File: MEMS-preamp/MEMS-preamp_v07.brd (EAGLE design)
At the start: 50 x 30.1 mm, 45 parts, among them IC1 DMN2400, IC2 BQ21040, IC3 BQ297X, IC4 SC4503, IC5 TPS7A49, IC6 OPA2134, J2 Battery, SW1 SPDT

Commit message: boards layed out
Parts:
- C1, C10, C2, C3, C7, C8: device adafruit:C0603 -> rcl:C0603
- C4: value 56nf -> 56nF; device adafruit:C0603 -> rcl:C0603
- C5: value 2.2pf -> 2.2pF; device adafruit:C0603 -> rcl:C0603
- C6: device SparkFun:EIA3528 -> rcl:C1206
- C9: value 10nF -> 10uF; device adafruit:C0603 -> rcl:C0603
- moved C6 37.7 mm to (8.00, 28.0)
- moved C13 32.6 mm to (37.8, 2.68)
- moved C5 30.8 mm to (37.9, 7.02), turned to 0 degrees
- moved C2 21.1 mm to (41.4, 20.4)
- moved C1 15.3 mm to (42.0, 11.0)
- moved C4 14.4 mm to (24.8, 8.20)
- moved C8 11.1 mm to (34.0, 20.5)
- moved R10 10.4 mm to (42.7, 23.9)
- moved R15 9.66 mm to (16.1, 1.79)
- moved R9 9.53 mm to (42.7, 27.4)
- moved C10 9.27 mm to (38.0, 11.0), turned to 0 degrees
- moved C3 8.73 mm to (15.0, 18.0), turned to 0 degrees
- moved C7 6.14 mm to (37.4, 20.5), turned to 0 degrees
- moved C12 5.75 mm to (16.1, 5.09)
- moved IC6 5.56 mm to (8.98, 3.52)
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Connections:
- net GND: now also C6.2; no longer C6.C
- net GND2: now also C2.1; no longer C2.2
- net N$18: now also C2.2; no longer C2.1
- net V+: now also C6.1; no longer C6.A
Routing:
- net N$1: track 9.46 -> 43.9 mm, vias 0 -> 3
- net GND: track 178.1 -> 209.5 mm, vias 4 -> 5
- net N$14: track 18.3 -> 43.0 mm, vias 2 -> 4
- net V+: track 90.0 -> 113.3 mm, vias 1 -> 3
- net N$7: track 22.8 -> 40.2 mm
- net N$9: track 17.4 -> 31.8 mm
- net GROU[: track 17.4 -> 31.6 mm
- net N$18: track 13.1 -> 23.0 mm, vias 3 -> 2
- net +12V: track 108.6 -> 99.0 mm
- net N$11: track 17.9 -> 10.0 mm, vias 1 -> 0
- net N$8: track 64.1 -> 71.5 mm, vias 3 -> 0
- net N$10: track 18.4 -> 25.4 mm
- net N$5: track 8.00 -> 15.0 mm
- net GND2: track 62.7 -> 69.5 mm, vias 1 -> 4
- net N$13: track 17.5 -> 23.5 mm
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
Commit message: piezo and mems preamps updates
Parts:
- C11: value 10uF -> 0.1uF
- POT1: value 50k -> 20K
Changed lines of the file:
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@@
 <?xml version="1.0" encoding="utf-8"?>
 <!DOCTYPE eagle SYSTEM "eagle.dtd">
-<eagle version="8.5.0">
+<eagle version="8.2.2">
 <drawing>
 <settings>
 <setting alwaysvectorfont="no"/>
-<setting keepoldvectorfont="yes"/>
 <setting verticaltext="up"/>
 </settings>
@@
 <param name="dpMaxLengthDifference" value="10mm"/>
 <param name="dpGapFactor" value="2.5"/>
+<param name="checkGrid" value="0"/>
 <param name="checkAngle" value="0"/>
 <param name="checkFont" value="1"/>
 <param name="checkRestrict" value="1"/>
-<param name="checkStop" value="0"/>
-<param name="checkValues" value="0"/>
 <param name="useDiameter" value="13"/>
 <param name="maxErrors" value="50"/>
@@
 <attribute name="VALUE" x="15.785" y="0.36" size="0.6604" layer="27" font="vector" ratio="15"/>
 </element>
-<element name="POT1" library="CMU-ArtFab" package="PTV112" value="50k" x="25" y="15" smashed="yes" rot="MR0">
+<element name="POT1" library="CMU-ArtFab" package="PTV112" value="20K" x="25" y="15" smashed="yes" rot="MR0">
 <attribute name="AVAILABILITY" value="Unavailable" x="25" y="15" size="1.778" layer="28" rot="MR0" display="off"/>
 <attribute name="DESCRIPTION" value=" Alt# Tce-10111410 " x="25" y="15" size="1.778" layer="28" rot="MR0" display="off"/>
@@
 <attribute name="VALUE" x="41.609" y="22.437" size="0.6604" layer="27" font="vector" ratio="15"/>
 </element>
-<element name="C11" library="adafruit" package="C0603" value="10uF" x="32.754" y="27.822" smashed="yes">
+<element name="C11" library="adafruit" package="C0603" value="0.1uF" x="32.754" y="27.822" smashed="yes">
 <attribute name="NAME" x="32.225" y="28.714" size="0.6604" layer="25" font="vector" ratio="15"/>
 <attribute name="VALUE" x="31.675" y="26.32" size="0.6604" layer="27" font="vector" ratio="15"/>
@@
 <attribute name="VALUE" x="8.73" y="16.32" size="0.6604" layer="27" font="vector" ratio="15"/>
 </element>
-<element name="C6" library="rcl" library_urn="urn:adsk.eagle:library:334" package="C1206" package3d_urn="urn:adsk.eagle:package:23618/2" value="68uF" x="8" y="28" smashed="yes">
+<element name="C6" library="rcl" library_urn="urn:adsk.eagle:library:334" package="C1206" value="68uF" x="8" y="28" smashed="yes">
 <attribute name="NAME" x="6.73" y="29.27" size="0.6604" layer="25" font="vector" ratio="15"/>
 <attribute name="SPICEPREFIX" value="C" x="8" y="28" size="0.6604" layer="27" font="vector" ratio="15" display="off"/>
 <attribute name="VALUE" x="6.73" y="25.46" size="0.6604" layer="27" font="vector" ratio="15"/>
 </element>
-<element name="C3" library="rcl" library_urn="urn:adsk.eagle:library:334" package="C0603" package3d_urn="urn:adsk.eagle:package:23616/2" value="10uF" x="15" y="18" smashed="yes">
+<element name="C3" library="rcl" library_urn="urn:adsk.eagle:library:334" package="C0603" value="10uF" x="15" y="18" smashed="yes">
 <attribute name="NAME" x="14.365" y="18.635" size="0.6604" layer="25" font="vector" ratio="15"/>
 <attribute name="SPICEPREFIX" value="C" x="15" y="18" size="0.6604" layer="27" font="vector" ratio="15" display="off"/>
 <attribute name="VALUE" x="14.365" y="16.095" size="0.6604" layer="27" font="vector" ratio="15"/>
 </element>
-<element name="C4" library="rcl" library_urn="urn:adsk.eagle:library:334" package="C0603" package3d_urn="urn:adsk.eagle:package:23616/2" value="56nF" x="24.8" y="8.2" smashed="yes">
+<element name="C4" library="rcl" library_urn="urn:adsk.eagle:library:334" package="C0603" value="56nF" x="24.8" y="8.2" smashed="yes">
 <attribute name="NAME" x="24.165" y="8.835" size="0.6604" layer="25" font="vector" ratio="15"/>
 <attribute name="SPICEPREFIX" value="C" x="24.8" y="8.2" size="0.6604" layer="27" font="vector" ratio="15" display="off"/>
 <attribute name="VALUE" x="24.165" y="6.295" size="0.6604" layer="27" font="vector" ratio="15"/>
 </element>
-<element name="C5" library="rcl" library_urn="urn:adsk.eagle:library:334" package="C0603" package3d_urn="urn:adsk.eagle:package:23616/2" value="2.2pF" x="37.85" y="7.02" smashed="yes">
+<element name="C5" library="rcl" library_urn="urn:adsk.eagle:library:334" package="C0603" value="2.2pF" x="37.85" y="7.02" smashed="yes">
 <attribute name="NAME" x="37.215" y="7.655" size="0.6604" layer="25" font="vector" ratio="15"/>
 <attribute name="SPICEPREFIX" value="C" x="37.85" y="7.02" size="0.6604" layer="27" font="vector" ratio="15" display="off"/>
 <attribute name="VALUE" x="36.685" y="5.585" size="0.6604" layer="27" font="vector" ratio="15"/>
 </element>
-<element name="C1" library="rcl" library_urn="urn:adsk.eagle:library:334" package="C0603" package3d_urn="urn:adsk.eagle:package:23616/2" value="10uF" x="42" y="11" smashed="yes">
+<element name="C1" library="rcl" library_urn="urn:adsk.eagle:library:334" package="C0603" value="10uF" x="42" y="11" smashed="yes">
 <attribute name="NAME" x="41.365" y="11.635" size="0.6604" layer="25" font="vector" ratio="15"/>
 <attribute name="SPICEPREFIX" value="C" x="42" y="11" size="0.6604" layer="27" font="vector" ratio="15" display="off"/>
 <attribute name="VALUE" x="40.965" y="9.475" size="0.6604" layer="27" font="vector" ratio="15"/>
 </element>
-<element name="C2" library="rcl" library_urn="urn:adsk.eagle:library:334" package="C0603" package3d_urn="urn:adsk.eagle:package:23616/2" value="0.1uF" x="41.43" y="20.42" smashed="yes">
+<element name="C2" library="rcl" library_urn="urn:adsk.eagle:library:334" package="C0603" value="0.1uF" x="41.43" y="20.42" smashed="yes">
 <attribute name="NAME" x="40.795" y="21.055" size="0.6604" layer="25" font="vector" ratio="15"/>
 <attribute name="SPICEPREFIX" value="C" x="41.43" y="20.42" size="0.6604" layer="27" font="vector" ratio="15" display="off"/>
 <attribute name="VALUE" x="40.255" y="19.015" size="0.6604" layer="27" font="vector" ratio="15"/>
 </element>
-<element name="C7" library="rcl" library_urn="urn:adsk.eagle:library:334" package="C0603" package3d_urn="urn:adsk.eagle:package:23616/2" value="10uF" x="37.42" y="20.46" smashed="yes">
+<element name="C7" library="rcl" library_urn="urn:adsk.eagle:library:334" package="C0603" value="10uF" x="37.42" y="20.46" smashed="yes">
 <attribute name="NAME" x="36.785" y="21.095" size="0.6604" layer="25" font="vector" ratio="15"/>
 <attribute name="SPICEPREFIX" value="C" x="37.42" y="20.46" size="0.6604" layer="27" font="vector" ratio="15" display="off"/>
 <attribute name="VALUE" x="36.385" y="18.955" size="0.6604" layer="27" font="vector" ratio="15"/>
 </element>
-<element name="C8" library="rcl" library_urn="urn:adsk.eagle:library:334" package="C0603" package3d_urn="urn:adsk.eagle:package:23616/2" value="10nF" x="33.97" y="20.46" smashed="yes">
+<element name="C8" library="rcl" library_urn="urn:adsk.eagle:library:334" package="C0603" value="10nF" x="33.97" y="20.46" smashed="yes">
 <attribute name="NAME" x="33.335" y="21.095" size="0.6604" layer="25" font="vector" ratio="15"/>
 <attribute name="SPICEPREFIX" value="C" x="33.97" y="20.46" size="0.6604" layer="27" font="vector" ratio="15" display="off"/>
 <attribute name="VALUE" x="32.885" y="19.005" size="0.6604" layer="27" font="vector" ratio="15"/>
 </element>
-<element name="C9" library="rcl" library_urn="urn:adsk.eagle:library:334" package="C0603" package3d_urn="urn:adsk.eagle:package:23616/2" value="10uF" x="34" y="11" smashed="yes">
+<element name="C9" library="rcl" library_urn="urn:adsk.eagle:library:334" package="C0603" value="10uF" x="34" y="11" smashed="yes">
 <attribute name="NAME" x="33.365" y="11.635" size="0.6604" layer="25" font="vector" ratio="15"/>
 <attribute name="SPICEPREFIX" value="C" x="34" y="11" size="0.6604" layer="27" font="vector" ratio="15" display="off"/>
 <attribute name="VALUE" x="32.965" y="9.545" size="0.6604" layer="27" font="vector" ratio="15"/>
 </element>
-<element name="C10" library="rcl" library_urn="urn:adsk.eagle:library:334" package="C0603" package3d_urn="urn:adsk.eagle:package:23616/2" value="10uF" x="38" y="11" smashed="yes">
+<element name="C10" library="rcl" library_urn="urn:adsk.eagle:library:334" package="C0603" value="10uF" x="38" y="11" smashed="yes">
 <attribute name="NAME" x="37.365" y="11.635" size="0.6604" layer="25" font="vector" ratio="15"/>
 <attribute name="SPICEPREFIX" value="C" x="38" y="11" size="0.6604" layer="27" font="vector" ratio="15" display="off"/>
@@
 <compatibility>
 <note version="8.2" severity="warning">
-Since Version 8.2, EAGLE supports online libraries. The ids
+Since Version 8.2, Eagle supports online libraries. The ids
 of those online libraries will not be understood (or retained)
 with this version.
 </note>
-<note version="8.3" severity="warning">
-Since Version 8.3, EAGLE supports URNs for individual library
-assets (packages, symbols, and devices). The URNs of those assets
-will not be understood (or retained) with this version.
-</note>
-<note version="8.3" severity="warning">
-Since Version 8.3, EAGLE supports the association of 3D packages
-with devices in libraries, schematics, and board files. Those 3D
-packages will not be understood (or retained) with this version.
-</note>
 </compatibility>

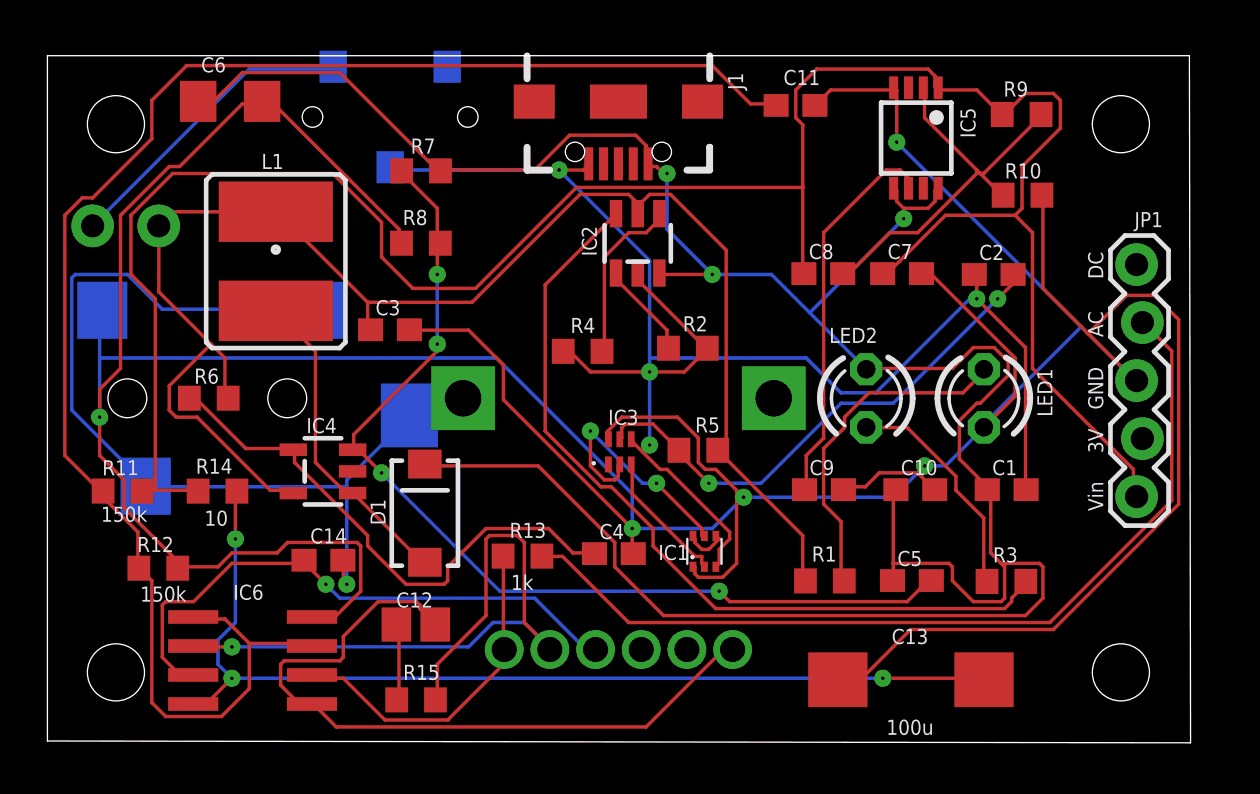
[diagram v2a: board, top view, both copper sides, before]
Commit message: piezo and mems preamps updates
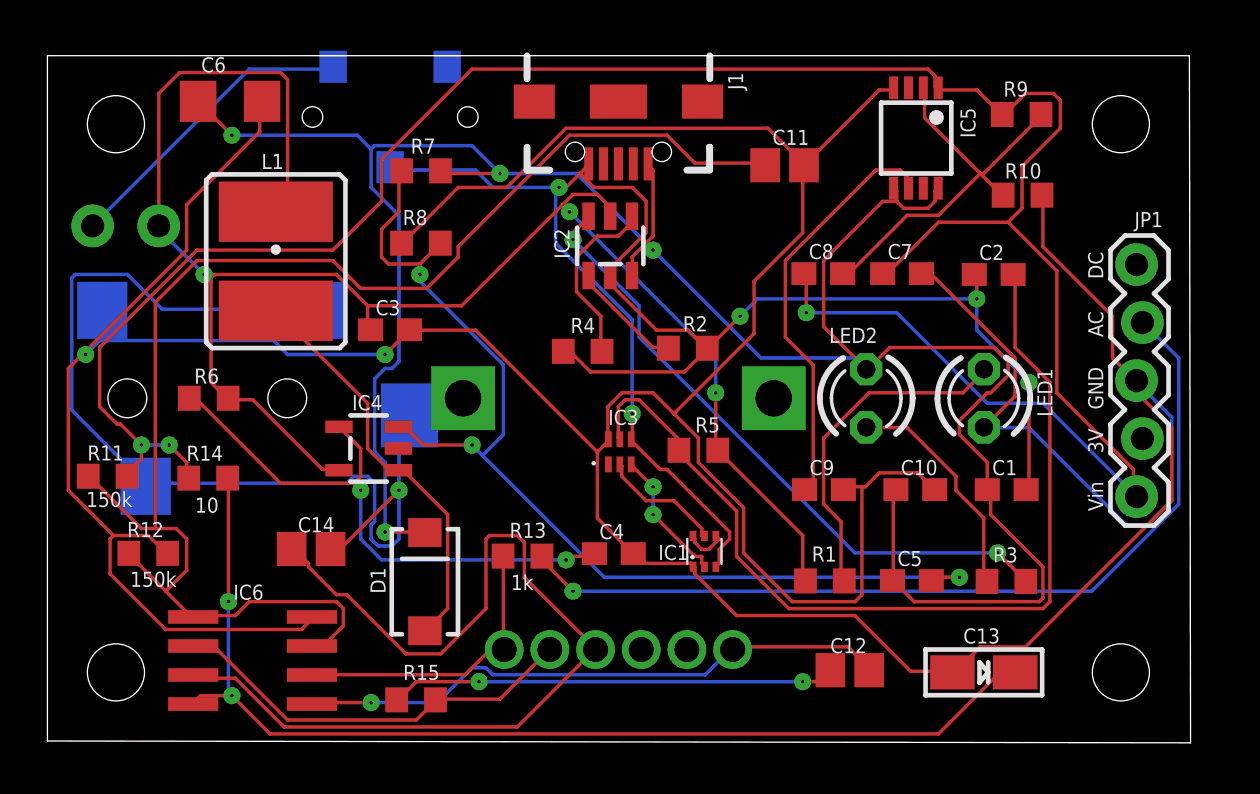
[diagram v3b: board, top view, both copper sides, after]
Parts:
- C11, C14: device adafruit:C0603 -> adafruit:C0805
- C13: value 100u -> 100uF; device rcl:CT7343 -> microbuilder:EIA3216-18/A-R
- moved C12 19.1 mm to (35.1, 3.10)
- moved C13 3.21 mm to (41.0, 3.00), turned to 0 degrees
- moved D1 3.00 mm to (16.5, 6.97)
- moved C11 2.66 mm to (32.3, 25.2)
- moved IC4 2.24 mm to (14.1, 12.8)
- moved IC2 1.21 mm to (24.6, 21.7)
- moved R11 0.92 mm to (2.64, 11.6)
- moved R12 0.78 mm to (4.42, 8.21)
- moved C14 0.73 mm to (11.5, 8.40)
- moved R14 0.70 mm to (7.04, 11.5)
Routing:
- net N$18: track 23.0 -> 40.9 mm, vias 2 -> 0
- net N$10: track 25.4 -> 42.2 mm, vias 1 -> 0
- net N$4: track 3.44 -> 19.5 mm, vias 0 -> 2
- net GROU[: track 31.6 -> 18.3 mm, vias 1 -> 0
- net N$8: track 71.5 -> 63.1 mm
- net VBAT: track 67.8 -> 75.9 mm, vias 0 -> 3
- net N$15: track 36.2 -> 28.1 mm, vias 0 -> 2
- net +12V: track 99.0 -> 106.3 mm, vias 0 -> 3
- net V+: track 113.3 -> 106.4 mm, vias 3 -> 4
- net N$9: track 31.8 -> 26.2 mm, vias 0 -> 1
- net N$7: track 40.2 -> 45.8 mm
- net N$20: track 10.7 -> 5.44 mm, vias 2 -> 0
- net N$12: track 14.0 -> 17.9 mm
- net N$1: track 43.9 -> 47.6 mm, vias 3 -> 2
- net GND2: track 69.5 -> 73.1 mm, vias 4 -> 5
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
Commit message: pizeo and mems
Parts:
- C9: value 10uF -> 10nF
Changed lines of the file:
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@@
 <?xml version="1.0" encoding="utf-8"?>
 <!DOCTYPE eagle SYSTEM "eagle.dtd">
-<eagle version="8.2.2">
+<eagle version="8.3.1">
 <drawing>
 <settings>
 <setting alwaysvectorfont="no"/>
+<setting keepoldvectorfont="yes"/>
 <setting verticaltext="up"/>
 </settings>
@@
 <attribute name="VALUE" x="32.885" y="19.005" size="0.6604" layer="27" font="vector" ratio="15"/>
 </element>
-<element name="C9" library="rcl" library_urn="urn:adsk.eagle:library:334" package="C0603" value="10uF" x="34" y="11" smashed="yes">
+<element name="C9" library="rcl" library_urn="urn:adsk.eagle:library:334" package="C0603" value="10nF" x="34" y="11" smashed="yes">
 <attribute name="NAME" x="33.365" y="11.635" size="0.6604" layer="25" font="vector" ratio="15"/>
 <attribute name="SPICEPREFIX" value="C" x="34" y="11" size="0.6604" layer="27" font="vector" ratio="15" display="off"/>
@@
 <compatibility>
 <note version="8.2" severity="warning">
-Since Version 8.2, Eagle supports online libraries. The ids
+Since Version 8.2, EAGLE supports online libraries. The ids
 of those online libraries will not be understood (or retained)
 with this version.

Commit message: pizeo and mems
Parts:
- L1: value 2.7mH -> 2.7uH
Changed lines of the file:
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@@
 <?xml version="1.0" encoding="utf-8"?>
 <!DOCTYPE eagle SYSTEM "eagle.dtd">
-<eagle version="8.3.1">
+<eagle version="8.5.0">
 <drawing>
 <settings>
@@
 <param name="dpMaxLengthDifference" value="10mm"/>
 <param name="dpGapFactor" value="2.5"/>
-<param name="checkGrid" value="0"/>
 <param name="checkAngle" value="0"/>
 <param name="checkFont" value="1"/>
 <param name="checkRestrict" value="1"/>
+<param name="checkStop" value="0"/>
+<param name="checkValues" value="0"/>
 <param name="useDiameter" value="13"/>
 <param name="maxErrors" value="50"/>
@@
 <attribute name="VALUE" x="4.46" y="16.27" size="0.8128" layer="28" ratio="10" rot="MR180"/>
 </element>
-<element name="L1" library="SparkFun-Passives" package="CR54-KIT" value="2.7mH" x="10" y="21" smashed="yes">
+<element name="L1" library="SparkFun-Passives" package="CR54-KIT" value="2.7uH" x="10" y="21" smashed="yes">
 <attribute name="NAME" x="9.37" y="25.04" size="0.6604" layer="25" font="vector" ratio="15"/>
 <attribute name="VALUE" x="8.73" y="16.32" size="0.6604" layer="27" font="vector" ratio="15"/>

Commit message: upates
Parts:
- moved C1 1.00 mm to (43.0, 11.0)
- moved C10 1.00 mm to (39.0, 11.0)
- moved C11 1.00 mm to (33.3, 25.2)
- moved C12 1.00 mm to (36.1, 3.10)
- moved C13 1.00 mm to (42.0, 3.00)
- moved C2 1.00 mm to (42.4, 20.4)
- moved C4 1.00 mm to (25.8, 8.20)
- moved C5 1.00 mm to (38.9, 7.02)
- moved C7 1.00 mm to (38.4, 20.5)
- moved C8 1.00 mm to (35.0, 20.5)
- moved C9 1.00 mm to (35.0, 11.0)
- moved IC1 1.00 mm to (29.8, 8.30)
- moved IC2 1.00 mm to (25.6, 21.7)
- moved IC3 1.00 mm to (26.1, 12.7)
- moved IC4 1.00 mm to (14.1, 11.8)
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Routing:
- net GND: track 208.1 -> 177.9 mm
- net +12V: track 106.3 -> 76.5 mm
- net N$7: track 45.8 -> 25.3 mm
- net N$15: track 28.1 -> 46.2 mm, vias 2 -> 0
- net N$8: track 63.1 -> 56.9 mm, vias 0 -> 2
- net N$14: track 46.2 -> 52.1 mm
- net V+: track 106.4 -> 100.8 mm, vias 4 -> 5
- net N$3: track 38.9 -> 43.9 mm, vias 1 -> 0
- net VBAT: track 75.9 -> 78.0 mm
- net N$10: track 42.2 -> 44.3 mm
- net N$4: track 19.5 -> 21.3 mm
- net GND2: track 73.1 -> 74.8 mm, vias 5 -> 4
- net N$18: track 40.9 -> 39.4 mm
- net N$5: track 13.0 -> 14.0 mm
- net N$12: track 17.9 -> 16.9 mm
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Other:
- board size 50 x 30.1 mm -> 51 x 30 mm
